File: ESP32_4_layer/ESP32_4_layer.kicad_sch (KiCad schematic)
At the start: 27 parts, among them J1 SS-52400-003, J2 JST_S2B-PH-K-S_LF__SN_, U1 MCP73871-4CC

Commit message: hierarchial label attached
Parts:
- C1, C2, C3, C4, C5, C6, C7: footprint (none) -> Capacitor_SMD:C_0805_2012Metric
- C8: footprint (none) -> Own_Library:T491A_Tantalum_Capacitor
- D1: footprint (none) -> Own_Library:Blue_Led_
- D2: footprint (none) -> Own_Library:Green_led_LTST-C170GKT
- D3, D4: footprint (none) -> Own_Library:Red_Led
- F1: footprint (none) -> Own_Library:Belfuse_FUSC3225X100N
- R1, R10, R2, R3, R4, R5, R6, R7, R8, R9: footprint (none) -> Resistor_SMD:R_0805_2012Metric
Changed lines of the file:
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@@
 			)
 		)
-		(property "Footprint" ""
+		(property "Footprint" "Own_Library:Green_led_LTST-C170GKT"
 			(at 233.68 68.58 0)
 			(effects
@@
 			)
 		)
-		(property "Footprint" ""
+		(property "Footprint" "Own_Library:Red_Led"
 			(at 233.68 63.5 0)
 			(effects
@@
 			)
 		)
-		(property "Footprint" ""
+		(property "Footprint" "Resistor_SMD:R_0805_2012Metric"
 			(at 166.37 55.118 90)
 			(effects
@@
 			)
 		)
-		(property "Footprint" ""
+		(property "Footprint" "Capacitor_SMD:C_0805_2012Metric"
 			(at 113.3348 45.72 0)
 			(effects
@@
 			)
 		)
-		(property "Footprint" ""
+		(property "Footprint" "Own_Library:T491A_Tantalum_Capacitor"
 			(at 120.3452 114.3 0)
 			(effects
@@
 			)
 		)
-		(property "Footprint" ""
+		(property "Footprint" "Capacitor_SMD:C_0805_2012Metric"
 			(at 55.5752 116.84 0)
 			(effects
@@
 			)
 		)
-		(property "Footprint" ""
+		(property "Footprint" "Capacitor_SMD:C_0805_2012Metric"
 			(at 170.4848 29.21 0)
 			(effects
@@
 			)
 		)
-		(property "Footprint" ""
+		(property "Footprint" "Resistor_SMD:R_0805_2012Metric"
 			(at 173.99 60.198 90)
 			(effects
@@
 			)
 		)
-		(property "Footprint" ""
+		(property "Footprint" "Capacitor_SMD:C_0805_2012Metric"
 			(at 45.4152 116.84 0)
 			(effects
@@
 			)
 		)
-		(property "Footprint" ""
+		(property "Footprint" "Capacitor_SMD:C_0805_2012Metric"
 			(at 110.1852 114.3 0)
 			(effects
@@
 			)
 		)
-		(property "Footprint" ""
+		(property "Footprint" "Resistor_SMD:R_0805_2012Metric"
 			(at 224.79 65.278 90)
 			(effects
@@
 			)
 		)
-		(property "Footprint" ""
+		(property "Footprint" "Resistor_SMD:R_0805_2012Metric"
 			(at 36.83 47.498 90)
 			(effects
@@
 			)
 		)
-		(property "Footprint" ""
+		(property "Footprint" "Resistor_SMD:R_0805_2012Metric"
 			(at 176.53 109.982 90)
 			(effects
@@
 			)
 		)
-		(property "Footprint" ""
+		(property "Footprint" "Resistor_SMD:R_0805_2012Metric"
 			(at 173.99 65.278 90)
 			(effects
@@
 			)
 		)
-		(property "Footprint" ""
+		(property "Footprint" "Resistor_SMD:R_0805_2012Metric"
 			(at 223.52 70.358 90)
 			(effects
@@
 			)
 		)
-		(property "Footprint" ""
+		(property "Footprint" "Own_Library:Red_Led"
 			(at 166.37 111.76 0)
 			(effects
@@
 			)
 		)
-		(property "Footprint" ""
+		(property "Footprint" "Capacitor_SMD:C_0805_2012Metric"
 			(at 229.87 44.7548 0)
 			(effects
@@
 			)
 		)
-		(property "Footprint" ""
+		(property "Footprint" "Resistor_SMD:R_0805_2012Metric"
 			(at 101.6 47.498 90)
 			(effects
@@
 			)
 		)
-		(property "Footprint" ""
+		(property "Footprint" "Capacitor_SMD:C_0805_2012Metric"
 			(at 229.87 37.1348 0)
 			(effects
@@
 			)
 		)
-		(property "Footprint" ""
+		(property "Footprint" "Resistor_SMD:R_0805_2012Metric"
 			(at 223.52 60.198 90)
 			(effects
@@
 			)
 		)
-		(property "Footprint" ""
+		(property "Footprint" "Resistor_SMD:R_0805_2012Metric"
 			(at 166.37 50.038 90)
 			(effects
@@
 			)
 		)
-		(property "Footprint" ""
+		(property "Footprint" "Own_Library:Belfuse_FUSC3225X100N"
 			(at 123.19 41.91 0)
 			(effects
@@
 			)
 		)
-		(property "Footprint" ""
+		(property "Footprint" "Own_Library:Blue_Led_"
 			(at 233.68 58.42 0)
 			(effects

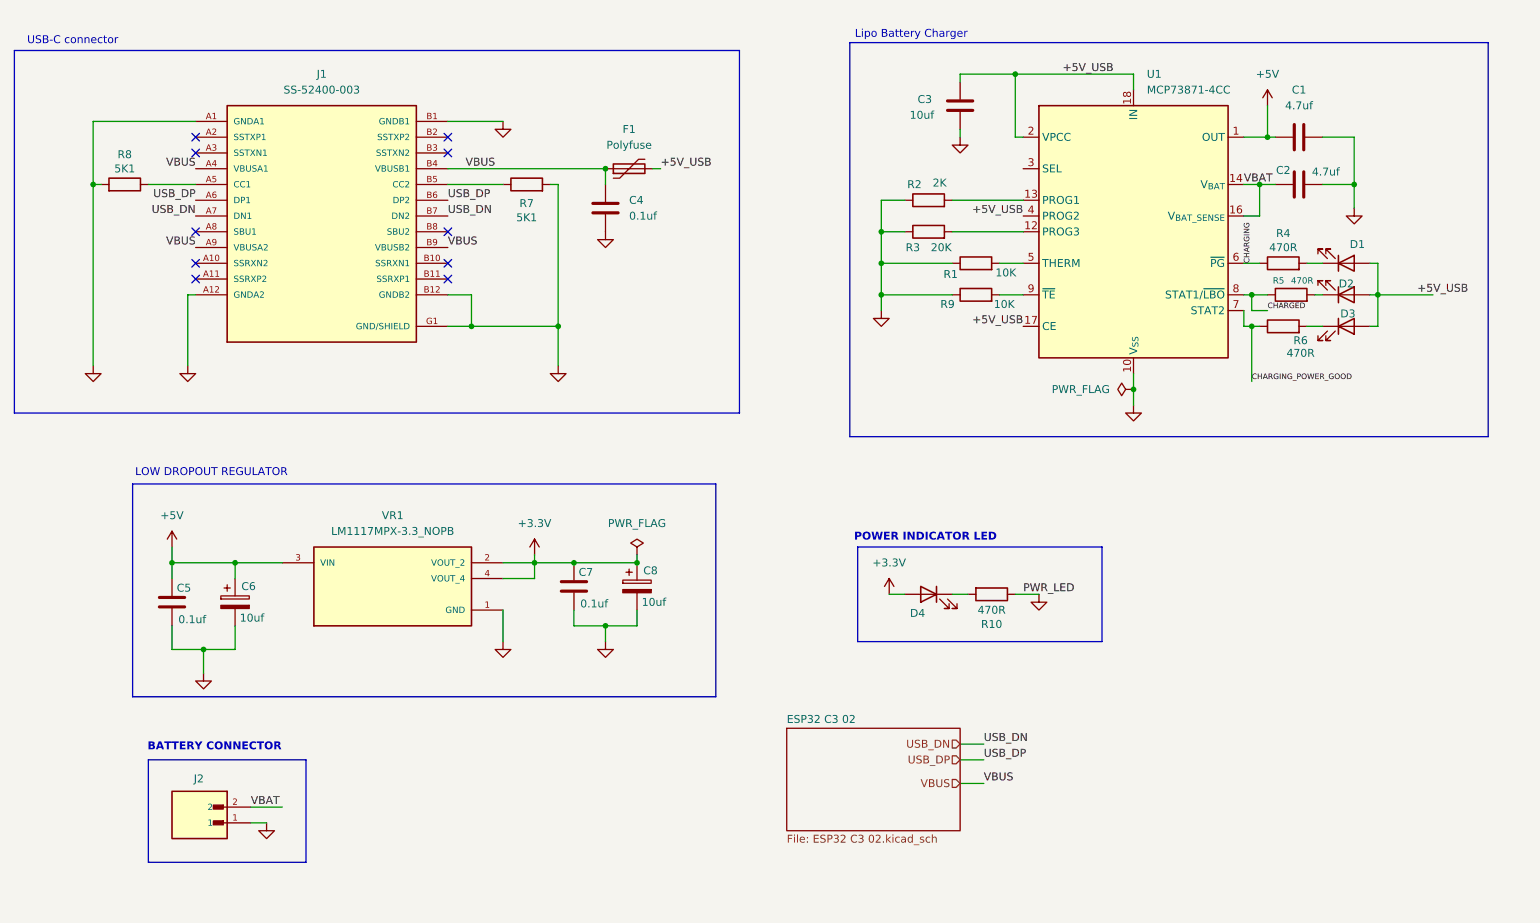
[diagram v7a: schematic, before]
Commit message: PCB Stack up, netlist and constrainsts applied
Signed-off-by: jayaraj <jayarajemengineer@gmail.com>
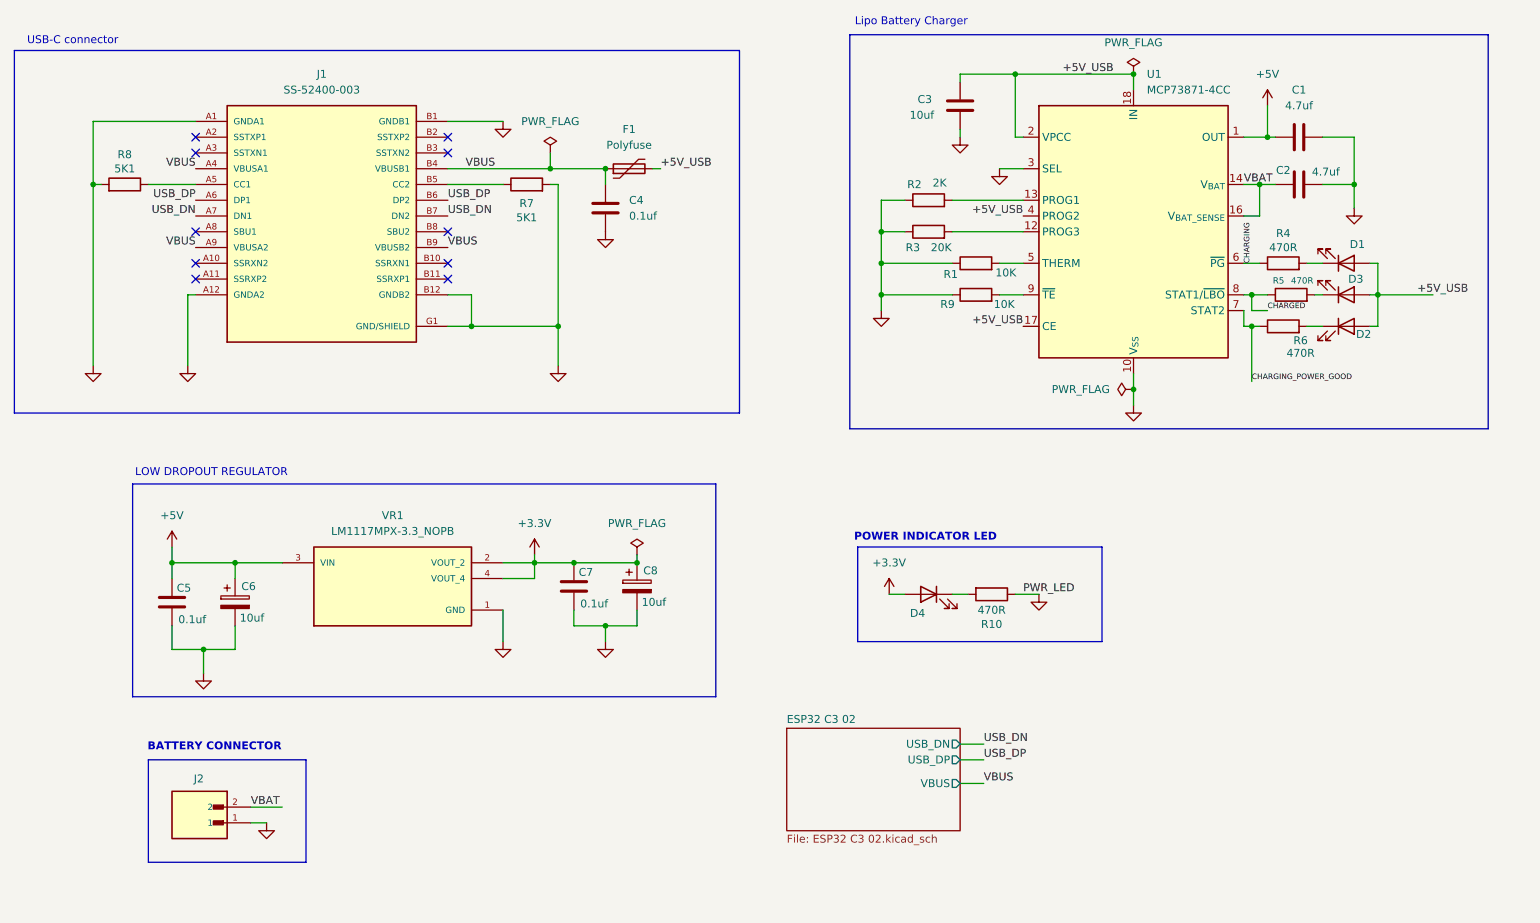
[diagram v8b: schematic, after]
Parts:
- D2: footprint Own_Library:Green_led_LTST-C170GKT -> Own_Library:Red_Led
- D3: footprint Own_Library:Red_Led -> Own_Library:Green_led_LTST-C170GKT
- J1: footprint SS-52400-003:BELFUSE_SS-52400-003 -> Own_Library:BELFUSE_SS-52400-003
- J2: footprint S2B-PH-K-S_LF__SN_:JST_S2B-PH-K-S_LF__SN_ -> Own_Library:JST_S2B-PH-K-S_LF__SN_
- VR1: footprint LM1117MPX-3.3_NOPB:VREG_LM1117MPX-3.3_NOPB -> Own_Library:LM1117MPX-3.3_NOPB
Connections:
- net GND: now also U1.3 (SEL)
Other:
- sheet ESP32 C3 02 ports: added USB_DN, USB_DP, VBUS; removed none
